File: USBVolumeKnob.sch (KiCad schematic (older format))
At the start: 25 parts, among them J1 Conn_01x10_Male, SW1 SW_Push, SW2 SW_Push, U1 PEC12R-4xxxF

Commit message: Added custom library components and 3D data
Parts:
- J1: footprint Connector_PinHeader_2.54mm:PinHeader_1x10_P2.54mm_Vertical -> USBVolumeKnob:PinHeader_1x10_P2.54mm_Vertical
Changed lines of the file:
@@
 $EndComp
 Connection ~ 6000 1500
-$Comp
-L Connector:Conn_01x10_Male J1
-U 1 1 60AE72D6
-P 7300 4400
-F 0 "J1" H 7408 4981 50  0000 C CNN
-F 1 "Conn_01x10_Male" H 7408 4890 50  0000 C CNN
-F 2 "Connector_PinHeader_2.54mm:PinHeader_1x10_P2.54mm_Vertical" H 7300 4400 50  0001 C CNN
-F 3 "~" H 7300 4400 50  0001 C CNN
-	1    7300 4400
-	1    0    0    -1
-$EndComp
 Wire Wire Line
 	7500 4300 8000 4300
@@
 $EndComp
 Connection ~ 9500 5000
+$Comp
+L Connector:Conn_01x10_Male J1
+U 1 1 60AE72D6
+P 7300 4400
+F 0 "J1" H 7408 4981 50  0000 C CNN
+F 1 "Conn_01x10_Male" H 7408 4890 50  0000 C CNN
+F 2 "USBVolumeKnob:PinHeader_1x10_P2.54mm_Vertical" H 7300 4400 50  0001 C CNN
+F 3 "~" H 7300 4400 50  0001 C CNN
+	1    7300 4400
+	1    0    0    -1
+$EndComp
 $EndSCHEMATC

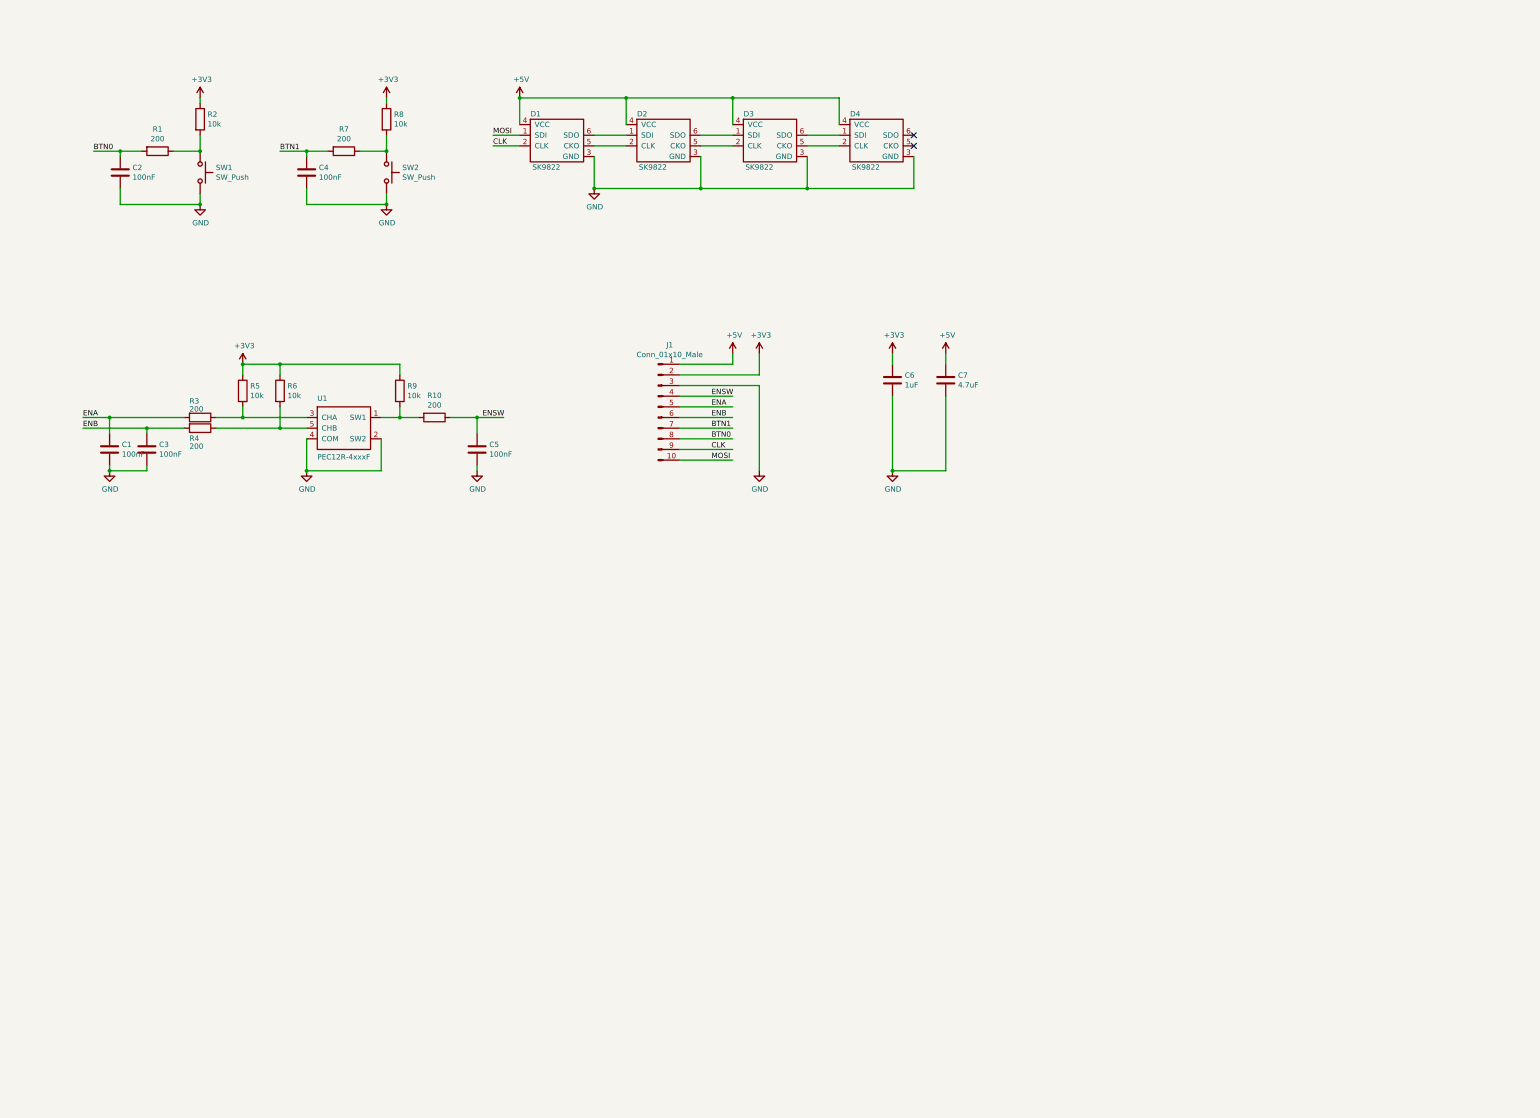
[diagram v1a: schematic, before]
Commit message: Schamatic complete, component placement complete
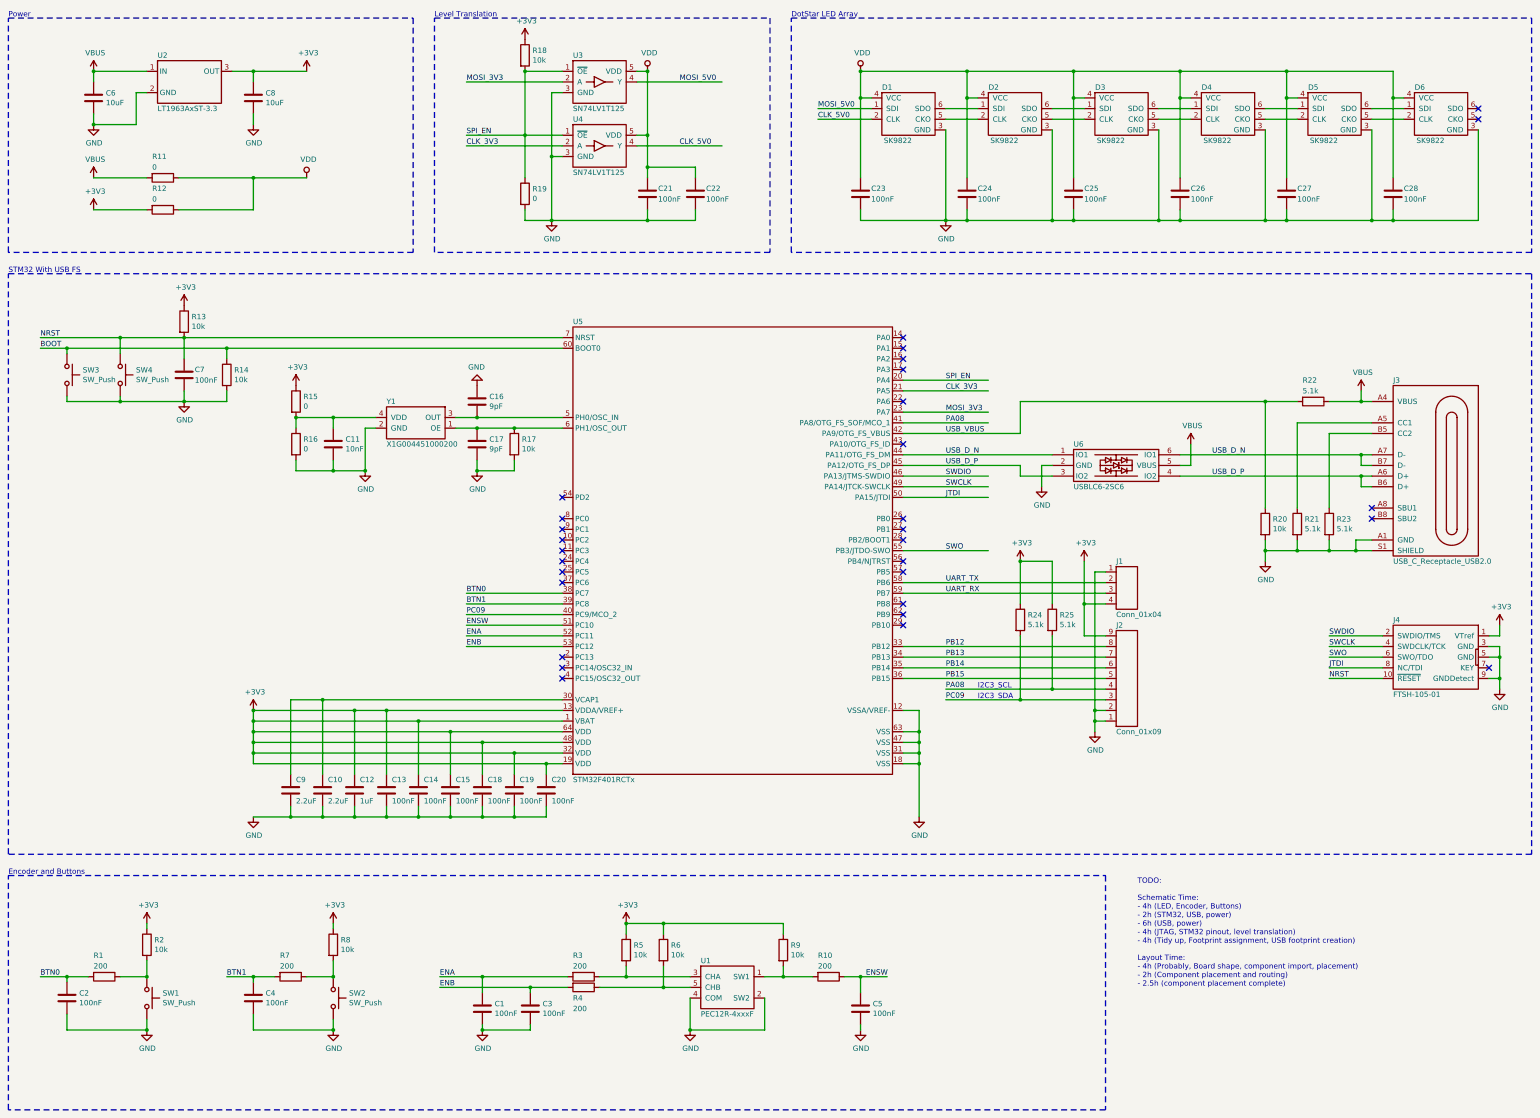
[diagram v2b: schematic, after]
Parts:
- removed J1: Conn_01x10_Male, USBVolumeKnob:PinHeader_1x10_P2.54mm_Vertical, symbol Connector:Conn_01x10_Male
- added C10, C9: 2.2uF, Capacitor_SMD:C_0805_2012Metric_Pad1.15x1.40mm_HandSolder, symbol Device:C
- added C11: 10nF, Capacitor_SMD:C_0603_1608Metric_Pad1.05x0.95mm_HandSolder, symbol Device:C
- added C12: 1uF, Capacitor_SMD:C_0603_1608Metric_Pad1.05x0.95mm_HandSolder, symbol Device:C
- added C13, C14, C15, C18, C19, C20, C21, C22, C23, C24, C25, C26, C27, C28: 100nF, Capacitor_SMD:C_0603_1608Metric_Pad1.05x0.95mm_HandSolder, symbol Device:C
- added C16, C17: 9pF, Capacitor_SMD:C_0402_1005Metric, symbol Device:C
- added C8: 10uF, Capacitor_SMD:C_0805_2012Metric_Pad1.15x1.40mm_HandSolder, symbol Device:C
- added D5, D6: SK9822, LED_SMD:LED_RGB_5050-6, symbol USBVolumeKnob:SK9822
- added J1: Conn_01x04, Connector_Molex:Molex_PicoBlade_53261-0471_1x04-1MP_P1.25mm_Horizontal, symbol USBVolumeKnob:Conn_01x04
- added J2: Conn_01x09, Connector_Molex:Molex_PicoBlade_53261-0971_1x09-1MP_P1.25mm_Horizontal, symbol USBVolumeKnob:Conn_01x09
- added J3: USB_C_Receptacle_USB2.0, USBVolumeKnob:USB_C_Receptacle_Amphenol_12402012E212A, symbol USBVolumeKnob:USB_C_Receptacle_USB2.0
- added J4: FTSH-105-01, USBVolumeKnob:SAMTEC_FTSH-105-XX-X-DV, symbol USBVolumeKnob:Conn_ARM_JTAG_SWD_10
- added R11, R12, R15, R16, R19: 0, Resistor_SMD:R_0603_1608Metric_Pad1.05x0.95mm_HandSolder, symbol Device:R
- added R13, R14, R17, R18, R20: 10k, Resistor_SMD:R_0603_1608Metric_Pad1.05x0.95mm_HandSolder, symbol Device:R
- added R21, R22, R23, R24, R25: 5.1k, Resistor_SMD:R_0603_1608Metric_Pad1.05x0.95mm_HandSolder, symbol Device:R
- added SW3, SW4: SW_Push, Button_Switch_SMD:SW_SPST_B3U-1000P, symbol Switch:SW_Push
- added U2: LT1963AxST-3.3, Package_TO_SOT_SMD:SOT-223-3_TabPin2, symbol USBVolumeKnob:LT1963AxST-3.3
- added U3, U4: SN74LV1T125, Package_TO_SOT_SMD:SOT-23-5_HandSoldering, symbol USBVolumeKnob:SN74LV1T125
- added U5: STM32F401RCTx, Package_QFP:LQFP-64_10x10mm_P0.5mm, symbol USBVolumeKnob:STM32F401RCTx
- added U6: USBLC6-2SC6, Package_TO_SOT_SMD:SOT-23-6, symbol USBVolumeKnob:USBLC6-2SC6
- added Y1: X1G004451000200, Crystal:Crystal_SMD_5032-4Pin_5.0x3.2mm, symbol USBVolumeKnob:SG-5032
- C6: value 1uF -> 10uF; footprint Capacitor_SMD:C_0603_1608Metric_Pad1.05x0.95mm_HandSolder -> Capacitor_SMD:C_0805_2012Metric_Pad1.15x1.40mm_HandSolder
- C7: value 4.7uF -> 100nF; footprint Capacitor_SMD:C_0805_2012Metric_Pad1.15x1.40mm_HandSolder -> Capacitor_SMD:C_0603_1608Metric_Pad1.05x0.95mm_HandSolder
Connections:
- net labels added: BOOT, CLK_3V3, CLK_5V0, JTDI, MOSI_3V3, MOSI_5V0, NRST, PA08, PB12, PB13, PB14, PB15, PC09, SPI_EN, SWCLK, SWDIO, SWO, UART_RX, UART_TX, USB_D_N, USB_D_P, USB_VBUS, VBUS, VDD
- net labels removed: +5V, CLK, MOSI
- wire segments 88 -> 330
- no-connect marks 2 -> 30
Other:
- note added: "DotStar LED Array"
- note added: "Encoder and Buttons"
- note added: "I2C3_SCL"
- note added: "I2C3_SDA"
- note added: "Level Translation"
- note added: "Power"
- note added: "STM32 With USB FS"
- note added: "TODO:\n\nSchematic Time:\n- 4h (LED, Encoder, Buttons)\n- 2h (STM32, USB, power)\n- 6h (USB, power)\n- 4h (JTAG, STM32 pinout, level translation)\n- 4h (Tidy up, Footprint assignment, USB footprint creation)\n\nLayout Time:\n- 4h (Probably, Board shape, component import, placement)\n- 2h (Component placement and routing)\n- 2.5h (component placement complete)"
- moved on the sheet: C2, C3, C4, D3, D4, R1, R2, R3, R4, R5, R6, SW1

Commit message: Completed v02. Final schematic and layout.
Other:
- note removed: "TODO:\n\nSchematic Time:\n- 4h (LED, Encoder, Buttons)\n- 2h (STM32, USB, power)\n- 6h (USB, power)\n- 4h (JTAG, STM32 pinout, level translation)\n- 4h (Tidy up, Footprint assignment, USB footprint creation)\n\nLayout Time:\n- 4h (Probably, Board shape, component import, placement)\n- 2h (Component placement and routing)\n- 2.5h (component placement complete)"
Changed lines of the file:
@@
 Sheet 1 1
 Title "USBVolumeKnob"
-Date "2021-05-24"
-Rev "v01"
+Date "2021-10-26"
+Rev "v02"
 Comp ""
 Comment1 ""
@@
 Text Notes 1200 8800 0    50   ~ 0
 Encoder and Buttons
-Text Notes 11800 9850 0    50   ~ 0
-TODO:\n\nSchematic Time:\n- 4h (LED, Encoder, Buttons)\n- 2h (STM32, USB, power)\n- 6h (USB, power)\n- 4h (JTAG, STM32 pinout, level translation)\n- 4h (Tidy up, Footprint assignment, USB footprint creation)\n\nLayout Time:\n- 4h (Probably, Board shape, component import, placement)\n- 2h (Component placement and routing)\n- 2.5h (component placement complete)
 $Comp
 L Switch:SW_Push SW4
